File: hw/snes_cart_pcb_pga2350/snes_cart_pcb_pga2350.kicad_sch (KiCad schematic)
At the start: 9 parts, among them J1 snescart_SNESCART_EXT, J2 Conn_02x02_Counter_Clockwise, J3 Conn_02x02_Counter_Clockwise, J4 Conn_02x08_Counter_Clockwise, J5 Conn_02x09_Counter_Clockwise, SW1 SW_Push, U1 PGA2350

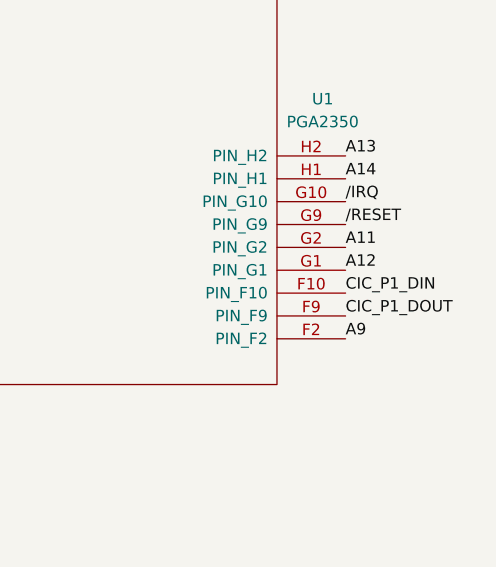
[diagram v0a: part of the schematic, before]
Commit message: (wip) initial support for cic on core1
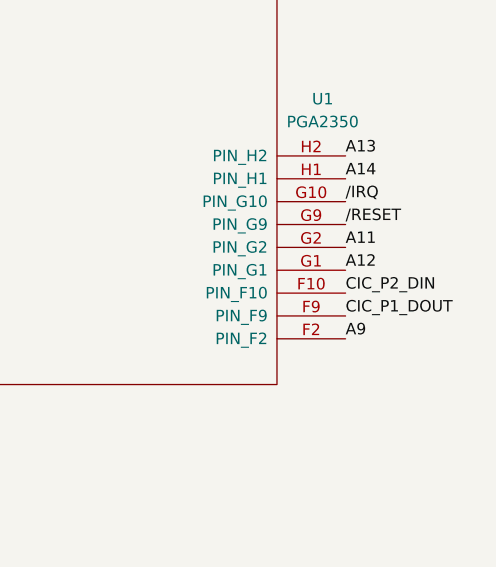
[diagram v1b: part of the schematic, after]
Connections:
- net CIC_P1_DIN is gone; now on net CIC_P2_DIN: U1.F10 (PIN_F10)
